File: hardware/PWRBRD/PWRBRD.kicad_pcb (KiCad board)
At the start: 2 copper layers, 66 parts, among them P1 USB_B, P2 CONN_01X03, Q1 Q_PMOS_GDS, Q2 Q_NPN_BCE, SW1 SW_PUSH, U1 ACT2803, U2 LM393, U3 TS30012, U4 SC189, U5 ZXSC420

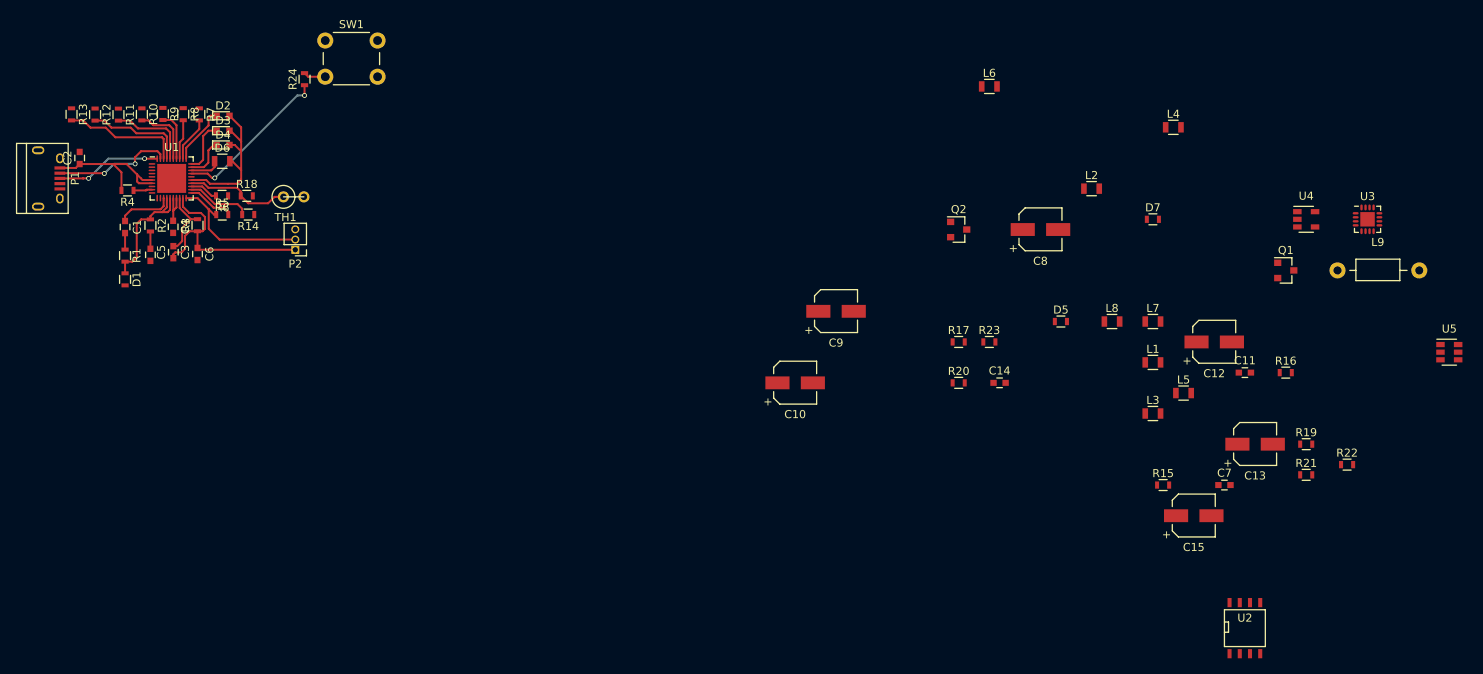
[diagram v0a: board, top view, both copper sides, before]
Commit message: Finished laying out and prettifying the BMS/Distribution Board.
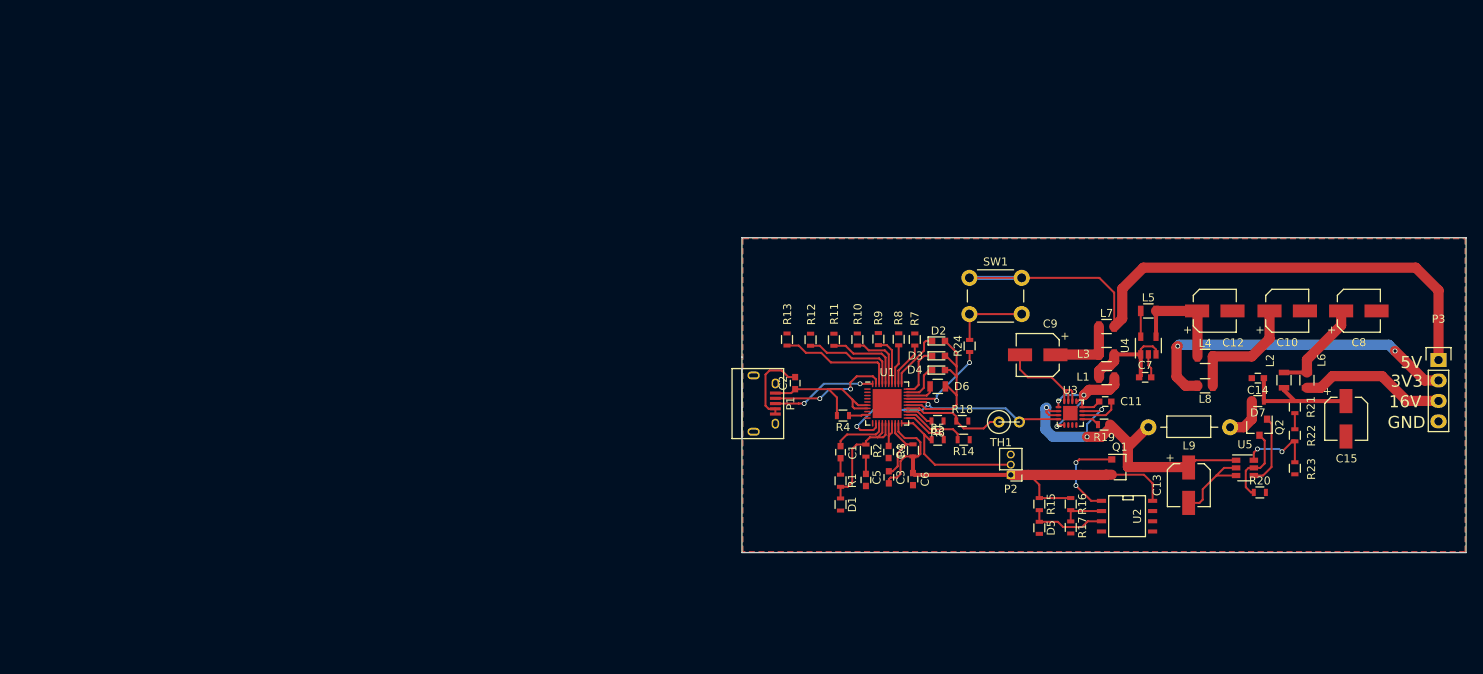
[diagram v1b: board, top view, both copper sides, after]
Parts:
- added P3: CONN_01X04, Pin_Headers:Pin_Header_Straight_1x04, F.Cu at (191.7, 102.6)
- moved C1 93.2 mm to (117.4, 114.0)
- moved C2 93.2 mm to (111.8, 105.4)
- moved C3 93.2 mm to (120.5, 117.5)
- moved C4 93.2 mm to (123.4, 114.0)
- moved C5 93.2 mm to (123.4, 117.2)
- moved C6 93.2 mm to (126.4, 117.4)
- moved D1 93.2 mm to (117.4, 120.5)
- moved P1 93.2 mm to (108.0, 108.0)
- moved P2 93.2 mm to (138.6, 116.8)
- moved R1 93.2 mm to (117.4, 117.6)
- moved R11 93.2 mm to (116.6, 100.1)
- moved R12 93.2 mm to (113.7, 100.0)
- moved R13 93.2 mm to (110.8, 100.0)
- moved R18 93.2 mm to (132.5, 110.2)
- moved R2 93.2 mm to (120.5, 113.8)
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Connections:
- SW1 pad 1: 5V -> 5V_FILT
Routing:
- net 5V_FILT: track 0.00 -> 84.8 mm
- net GND: track 0.00 -> 70.9 mm, vias 0 -> 2
- net VCC: track 0.00 -> 46.3 mm, vias 0 -> 3
- net 3V3_FILT: track 0.00 -> 41.2 mm, vias 0 -> 2
- net 7V4: track 26.8 -> 54.6 mm
- net VSW: track 0.00 -> 21.0 mm, vias 0 -> 3
- net 16V_FILT: track 0.00 -> 18.2 mm
- net 16V: track 0.00 -> 15.3 mm
- net Net-(C10-Pad1): track 0.00 -> 15.1 mm
- net 3V3: track 0.00 -> 14.0 mm
- net 5V: track 0.00 -> 13.7 mm
- net Net-(C8-Pad1): track 0.00 -> 12.3 mm
- net Net-(Q1-Pad1): track 0.00 -> 11.4 mm, vias 0 -> 2
- net SENSE: track 0.00 -> 9.81 mm
- net Net-(D5-Pad1): track 0.00 -> 9.74 mm
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- added copper zone on B.Cu, net GND
- added copper zone on F.Cu, net GND
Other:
- board outline added: 90 x 39.1 mm
- board text added: "1"
- board text added: "16V"
- board text added: "3V3"
- board text added: "5V"
- board text added: "February 24, 2017"
- board text added: "GND"
- board text added: "Power Breakout Board"

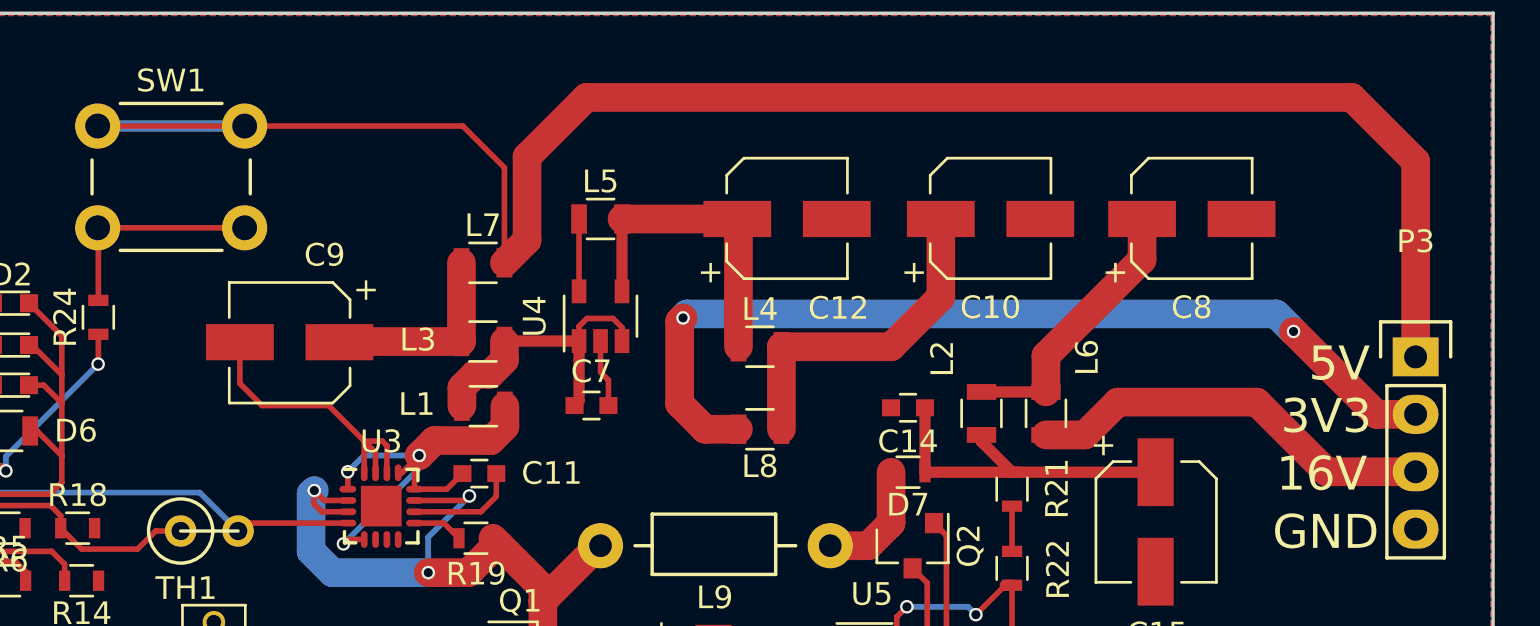
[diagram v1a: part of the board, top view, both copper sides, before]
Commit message: Removed some excessive Inductances.
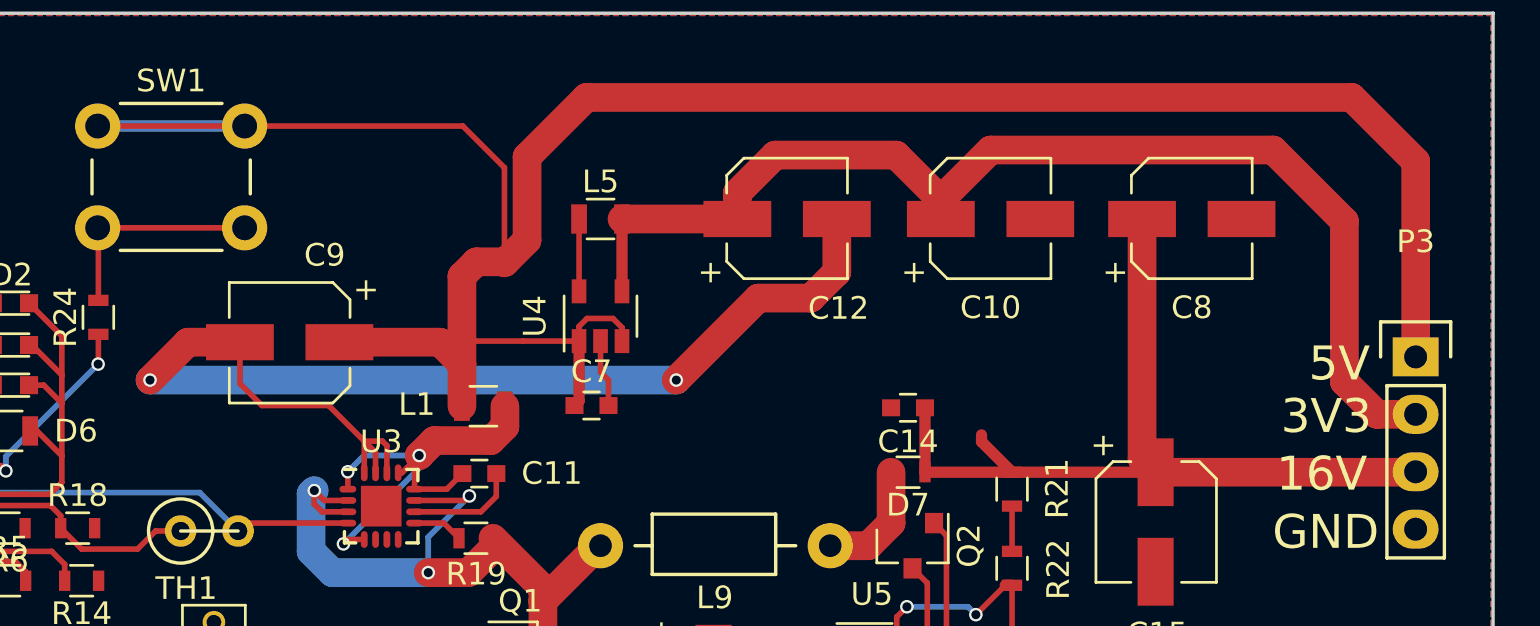
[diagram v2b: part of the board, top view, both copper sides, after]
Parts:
- removed L2, L3, L4: 27uH, Resistors_SMD:R_0805
- removed L6, L7, L8: 10uH, Resistors_SMD:R_0805
- R24: value R -> 1K
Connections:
- C10 pad 1: Net-(C10-Pad1) -> 3V3
- C8 pad 1: Net-(C8-Pad1) -> 16V
- C9 pad 1: Net-(C9-Pad1) -> 5V
- P3 pad 1: 5V_FILT -> 5V
- P3 pad 2: 3V3_FILT -> 3V3
- P3 pad 3: 16V_FILT -> 16V
- SW1 pad 1: 5V_FILT -> 5V
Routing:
- net 5V: track 13.7 -> 110.8 mm
- net 5V_FILT: track 84.8 -> 0.00 mm
- net 3V3_FILT: track 41.2 -> 0.00 mm, vias 2 -> 0
- net GND: track 70.9 -> 110.3 mm, vias 2 -> 4
- net 3V3: track 14.0 -> 51.8 mm
- net 16V: track 15.3 -> 38.2 mm
- net 16V_FILT: track 18.2 -> 0.00 mm
- net Net-(C10-Pad1): track 15.1 -> 0.00 mm
- net Net-(C8-Pad1): track 12.3 -> 0.00 mm
- net Net-(C9-Pad1): track 8.89 -> 0.00 mm
